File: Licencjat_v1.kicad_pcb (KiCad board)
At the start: 2 copper layers, 163 x 65 mm, 71 parts, among them J1 PV_IN_1, J10 SERIAL, J2 PV_IN_2, J3 AHT20 + BMP280, J4 VEML7700, J5 ADDITIONAL I2C, J6 RF_TRANSMITTER, J7 AVR-ISP-6, J8 GEIGER, J9 1_WIRE, Q1 AO3401A, Q10 2SC1945, Q11 AO3400A, Q2 BC846, Q3 AO3401A, Q4 AO3400A, Q5 AO3400A, Q6 AO3400A, Q7 AO3401A, Q8 AO3401A, Q9 2SC1945, U1 ATmega328P-A, U2 XC6206PxxxMR, U3 HT75xx-1-SOT89, Y1 Crystal_Small

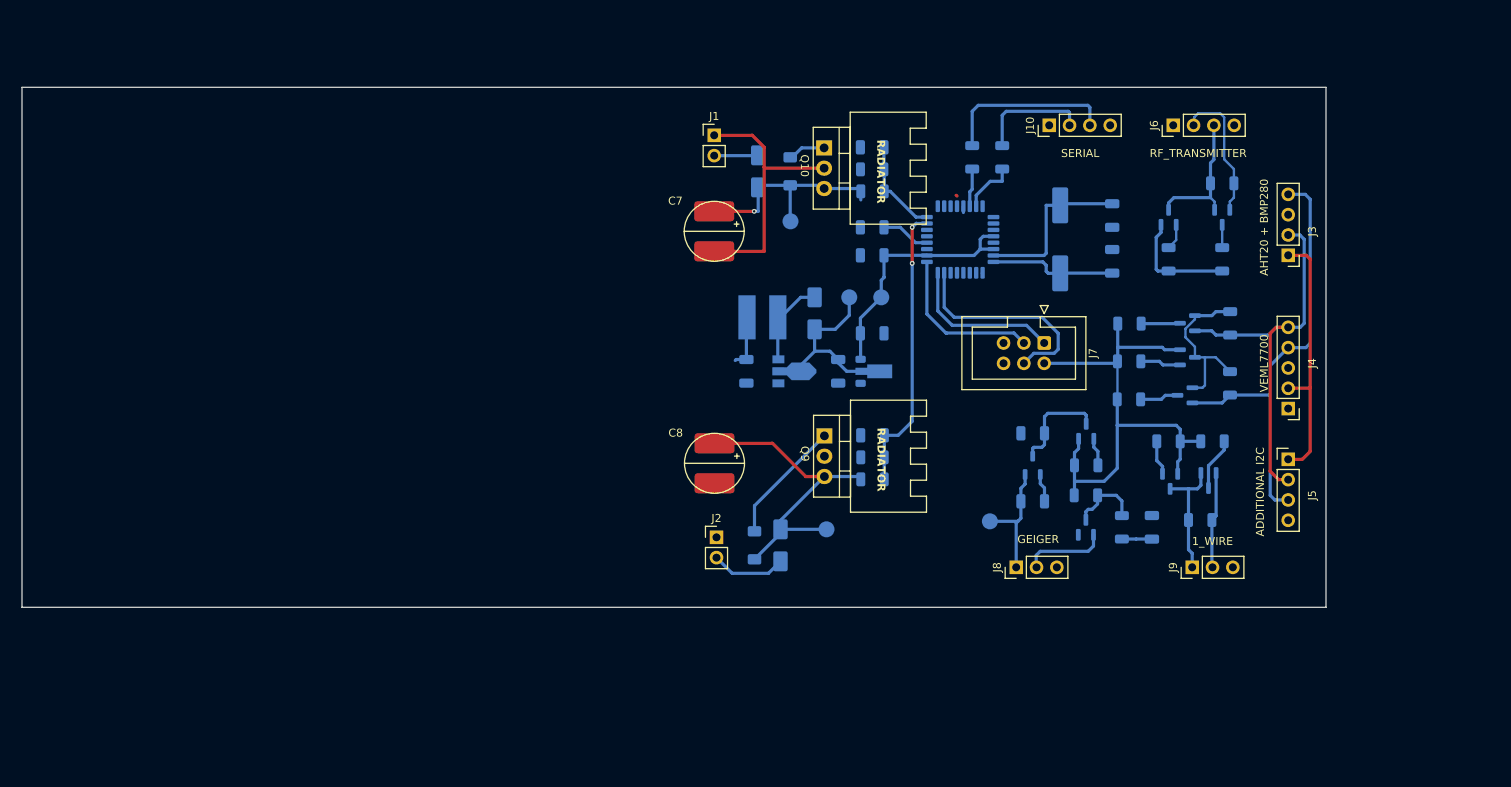
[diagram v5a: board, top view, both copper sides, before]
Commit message: Tracks placed
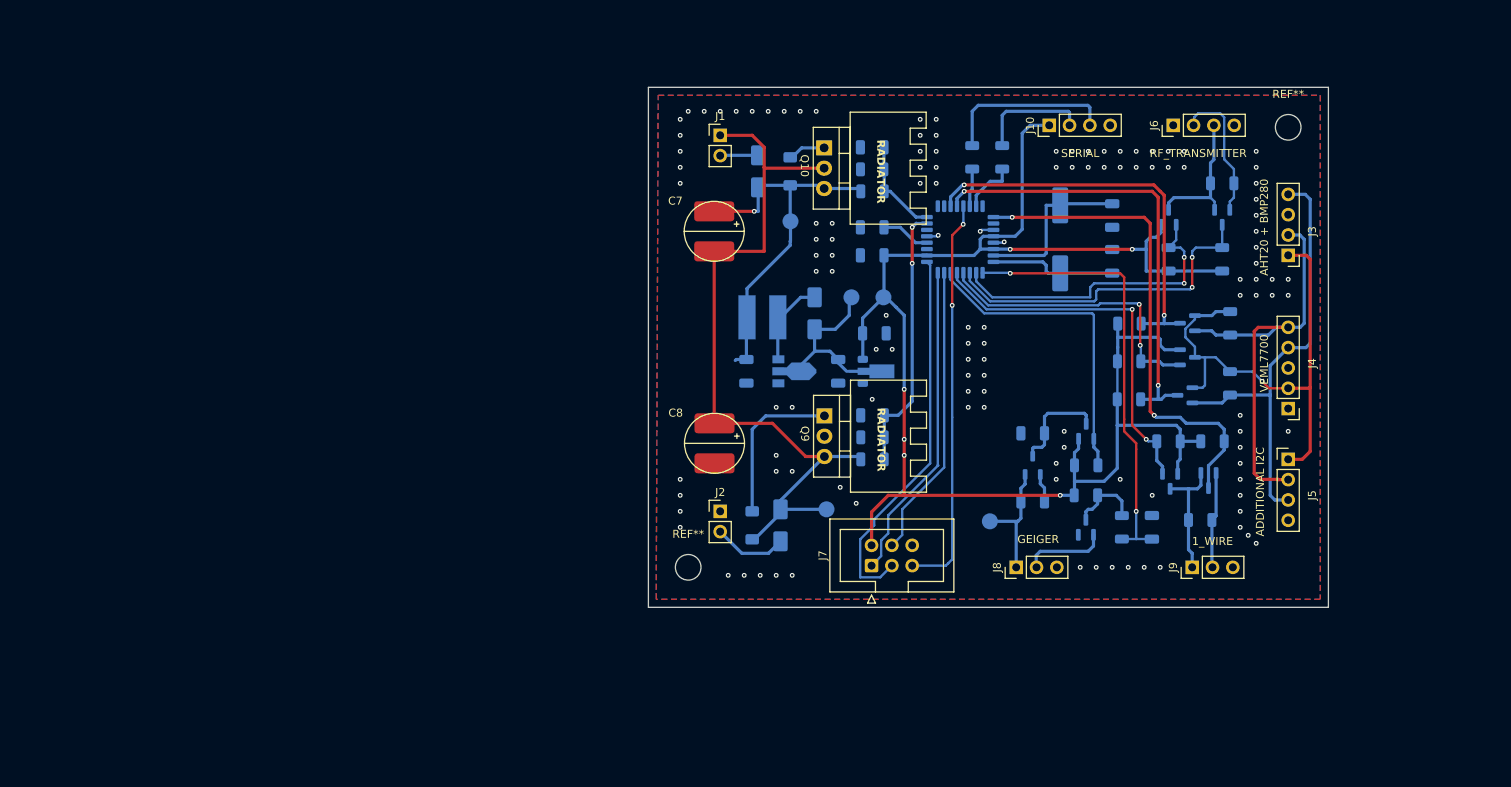
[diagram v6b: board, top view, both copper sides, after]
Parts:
- added REF**: MountingHole_3.2mm_M3, MountingHole:MountingHole_3.2mm_M3, F.Cu at (94.0, 85.0)
- added REF**: MountingHole_3.2mm_M3, MountingHole:MountingHole_3.2mm_M3, F.Cu at (169.0, 30.0)
- moved J7 35.2 mm to (116.9, 84.8), turned to 90 degrees
- moved J2 3.28 mm to (98.0, 78.0)
- moved D2 2.52 mm to (102.0, 79.8)
- moved C13 2.50 mm to (117.0, 66.0)
- moved C8 2.50 mm to (94.8, 65.7)
- moved D5 2.50 mm to (105.5, 79.8)
- moved Q9 2.50 mm to (114.3, 63.5)
- moved R10 2.50 mm to (117.0, 71.5)
- moved R11 2.50 mm to (117.0, 68.8)
- moved TP1 2.50 mm to (111.3, 77.8)
- moved J1 0.75 mm to (98.0, 31.0)
- moved C11 0.28 mm to (117.3, 55.8)
- moved TP3 0.28 mm to (114.4, 51.2)
- moved TP4 0.28 mm to (118.4, 51.2)
- moved U3 0.28 mm to (117.8, 60.5)
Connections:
- Q1 pad 1: /D4 -> /D10
- Q11 pad 3: /D10 -> /D7
- Q3 pad 1: /D7 -> /D6
- Q7 pad 1: /D8 -> /D9
- Q8 pad 1: /D6 -> /D8
- R20 pad 1: /D8 -> /D9
- R21 pad 1: /D10 -> /D7
- R3 pad 1: /D4 -> /D10
- R5 pad 1: /D7 -> /D6
- R9 pad 1: /D6 -> /D8
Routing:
- net /VCC: track 110.4 -> 199.9 mm, vias 0 -> 6
- net /1_WIRE: track 6.65 -> 61.7 mm, vias 0 -> 2
- net /SCL: track 4.95 -> 56.9 mm, vias 0 -> 2
- net /D5/T1: track 3.83 -> 55.1 mm, vias 0 -> 2
- net /~{RESET}: track 0.79 -> 50.0 mm, vias 0 -> 2
- net /D9: track 0.00 -> 47.1 mm, vias 0 -> 2
- net /SDA: track 4.87 -> 49.9 mm, vias 0 -> 2
- net /D7: track 3.24 -> 42.5 mm, vias 0 -> 2
- net /D10: track 2.90 -> 39.6 mm
- net /D6: track 5.07 -> 38.7 mm, vias 0 -> 2
- net /D8: track 4.37 -> 36.7 mm, vias 0 -> 2
- net /D13/SCK: track 20.2 -> 47.8 mm
- net /V_HALF_CAP: track 73.5 -> 94.3 mm
- net /D12/MISO: track 19.7 -> 40.1 mm
- net /V_CAP: track 34.5 -> 47.7 mm
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- added copper zone on B.Cu, net GND
- added copper zone on F.Cu, net GND
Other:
- board size 163 x 65 mm -> 85 x 65 mm
- board text added: "VCC"
- board text added: "V_BOOST"

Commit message: Labels placed
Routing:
- net /V_CAP: track 47.7 -> 46.3 mm
- net GND: vias 124 -> 127
- net /VCC: vias 6 -> 4
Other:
- board text added: "+"
- board text added: "VCC_GEIGER"
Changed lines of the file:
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@@
 		(at 94.75 39.2)
 		(property "Reference" "C7"
-			(at -2.35 0 0)
+			(at 2.5 9.3 0)
 			(unlocked yes)
 			(layer "F.SilkS")
@@
 			(layer "F.SilkS")
 		)
-		(fp_circle
-			(center 2.5 3.8)
-			(end 6.25 3.85)
+		(fp_arc
+			(start -0.357241 6.191133)
+			(mid -1.25 3.781118)
+			(end -0.381554 1.362236)
+			(stroke
+				(width 0.1)
+				(type default)
+			)
+			(layer "F.SilkS")
+		)
+		(fp_arc
+			(start 5.357526 1.371103)
+			(mid 6.250285 3.781118)
+			(end 5.381839 6.2)
 			(stroke
 				(width 0.1)
 				(type default)
 			)
-			(fill no)
 			(layer "F.SilkS")
 		)
@@
 			(polygon
 				(pts
-					(xy 101.000333 43) (xy 93.499667 43) (xy 93.6 43.85) (xy 93.75 44.4) (xy 94.2 45.2) (xy 94.9 45.95)
-					(xy 95.8 46.45) (xy 96.55 46.7) (xy 97.55 46.75) (xy 98.5 46.55) (xy 99.6 45.95) (xy 100.15 45.4)
-					(xy 100.8 44.3) (xy 101 43.45)
+					(xy 101.000332 43) (xy 101.000332 43.4) (xy 100.75 44.3) (xy 100.45 45) (xy 100.131837 45.4) (xy 99.85 45.4)
+					(xy 99.85 44.1) (xy 94.65 44.1) (xy 94.65 45.4) (xy 94.392759 45.391133) (xy 93.95 44.8) (xy 93.65 44)
+					(xy 93.55 43.3) (xy 93.500144 43) (xy 101.000426 43)
 				)
 			)
@@
 		(at 114.25 30 -90)
 		(property "Reference" "Q10"
-			(at 4.8 5.7 270)
+			(at -1 2.5 0)
 			(unlocked yes)
 			(layer "F.SilkS")
@@
 		(at 94.7875 65.7)
 		(property "Reference" "C8"
-			(at -2.35 0 0)
+			(at 2.4625 -2.2 0)
 			(unlocked yes)
 			(layer "F.SilkS")
@@
 			(layer "F.SilkS")
 		)
-		(fp_circle
-			(center 2.5 3.8)
-			(end 6.25 3.85)
+		(fp_arc
+			(start -0.357241 6.191133)
+			(mid -1.25 3.781118)
+			(end -0.381554 1.362236)
+			(stroke
+				(width 0.1)
+				(type default)
+			)
+			(layer "F.SilkS")
+		)
+		(fp_arc
+			(start 5.357526 1.371103)
+			(mid 6.250285 3.781118)
+			(end 5.381839 6.2)
 			(stroke
 				(width 0.1)
 				(type default)
 			)
-			(fill no)
 			(layer "F.SilkS")
 		)
@@
 			(polygon
 				(pts
-					(xy 101.037833 69.5) (xy 93.537167 69.5) (xy 93.6375 70.35) (xy 93.7875 70.9) (xy 94.2375 71.7)
-					(xy 94.9375 72.45) (xy 95.8375 72.95) (xy 96.5875 73.2) (xy 97.5875 73.25) (xy 98.5375 73.05) (xy 99.6375 72.45)
-					(xy 100.1875 71.9) (xy 100.8375 70.8) (xy 101.0375 69.95)
+					(xy 101.037832 69.5) (xy 101.037832 69.9) (xy 100.7875 70.8) (xy 100.4875 71.5) (xy 100.169337 71.9)
+					(xy 99.8875 71.9) (xy 99.8875 70.6) (xy 94.6875 70.6) (xy 94.6875 71.9) (xy 94.430259 71.891133)
+					(xy 93.9875 71.3) (xy 93.6875 70.5) (xy 93.5875 69.8) (xy 93.537644 69.5) (xy 101.037926 69.5)
 				)
 			)
@@
 		(tags "mountinghole M3")
 		(property "Reference" "REF**"
-			(at 0 -4.15 0)
+			(at -0.25 -5.5 0)
 			(layer "F.SilkS")
+			(hide yes)
 			(effects
 				(font
@@
 		(tags "Through hole pin header THT 1x02 2.54mm single row")
 		(property "Reference" "J2"
-			(at 0 -2.38 0)
+			(at -0.25 -2.5 0)
 			(layer "F.SilkS")
+			(hide yes)
 			(effects
 				(font
@@
 		)
 		(property "Value" "PV_IN_2"
-			(at 0 4.92 0)
-			(layer "F.Fab")
+			(at 0 -2.75 0)
+			(layer "F.SilkS")
 			(effects
 				(font
@@
 		)
 		(fp_text user "${REFERENCE}"
-			(at 0 1.27 90)
-			(layer "F.Fab")
+			(at 0 5 180)
+			(layer "F.SilkS")
 			(effects
 				(font
@@
 		(at 114.2875 63.5 -90)
 		(property "Reference" "Q9"
-			(at 4.8 5.7 270)
+			(at -1.5 2.2875 0)
 			(unlocked yes)
 			(layer "F.SilkS")
@@
 		)
 		(property "Value" "PV_IN_1"
-			(at 0 4.92 0)
-			(layer "F.Fab")
+			(at 0 5.25 0)
+			(layer "F.SilkS")
 			(effects
 				(font
@@
 		(tags "resistor")
 		(property "Reference" "R1"
-			(at 0 1.83 90)
+			(at 3.5 0 180)
 			(layer "B.SilkS")
 			(effects
@@
 		(tags "resistor")
 		(property "Reference" "R20"
-			(at 0 1.83 0)
+			(at 0.2125 -2 0)
 			(layer "B.SilkS")
 			(effects
@@
 		(tags "SOT TO_SOT_SMD")
 		(property "Reference" "U2"
-			(at 0 2.4 90)
+			(at -0.25 -3.5625 180)
 			(layer "B.SilkS")
 			(effects
@@
 		(tags "SOT TO_SOT_SMD")
 		(property "Reference" "Q2"
-			(at 0 2.4 90)
+			(at -3 0.0375 180)
 			(layer "B.SilkS")
 			(effects
@@
 		(tags "resistor")
 		(property "Reference" "R22"
-			(at 0 1.83 0)
+			(at -4 -0.25 0)
 			(layer "B.SilkS")
 			(effects
@@
 		(tags "resistor")
 		(property "Reference" "R19"
-			(at 0 1.83 0)
+			(at 0 2.0875 0)
 			(layer "B.SilkS")
 			(effects
@@
 		(tags "SOT TO_SOT_SMD")
 		(property "Reference" "Q11"
-			(at 0 2.4 90)
+			(at -0.25 -3.25 180)
 			(layer "B.SilkS")
 			(effects
@@
 		(tags "SOT TO_SOT_SMD")
 		(property "Reference" "Q5"
-			(at 0 2.4 0)
+			(at 3.09375 0 0)
 			(layer "B.SilkS")
 			(effects
@@
 		(tags "SOT TO_SOT_SMD")
 		(property "Reference" "Q7"
-			(at 0 2.4 90)
+			(at 0 2.9875 180)
 			(layer "B.SilkS")
 			(effects
@@
 		(tags "SOT TO_SOT_SMD")
 		(property "Reference" "Q6"
-			(at 0 2.4 90)
+			(at -0.15 -2.9625 180)
 			(layer "B.SilkS")
 			(effects
@@
 		(tags "resistor")
 		(property "Reference" "R2"
-			(at 0 1.83 90)
+			(at 3.5 0.25 180)
 			(layer "B.SilkS")
 			(effects
@@
 		(tags "capacitor")
 		(property "Reference" "C2"
-			(at 0 1.85 90)
+			(at -3.25 0 180)
 			(layer "B.SilkS")
 			(effects
@@
 			(at 0 1.998 0)
 			(layer "B.SilkS")
+			(hide yes)
 			(effects
 				(font
@@
 		(tags "SOT TO_SOT_SMD")
 		(property "Reference" "Q3"
-			(at 0 2.4 90)
+			(at 0 2.95 180)
 			(layer "B.SilkS")
 			(effects
@@
 		(tags "SOT TO_SOT_SMD")
 		(property "Reference" "Q8"
-			(at 0 2.4 0)
+			(at -3.15625 0.25 0)
 			(layer "B.SilkS")
 			(effects
@@
 		(tags "capacitor")
 		(property "Reference" "C14"
-			(at 0 1.85 90)
+			(at -3.25 0.0375 180)
 			(layer "B.SilkS")
 			(effects
@@
 		(tags "SOT TO_SOT_SMD")
 		(property "Reference" "Q4"
-			(at 0 2.4 0)
+			(at 3.15625 -0.0125 0)
 			(layer "B.SilkS")
 			(effects
@@
 		(tags "SOT TO_SOT_SMD")
 		(property "Reference" "Q1"
-			(at 0 2.4 90)
+			(at 0 3.25 180)
 			(layer "B.SilkS")
 			(effects
@@
 		(tags "resistor")
 		(property "Reference" "R14"
-			(at 0 1.83 90)
+			(at 0 2.75 180)
 			(layer "B.SilkS")
 			(effects
@@
 		(tags "resistor")
 		(property "Reference" "R4"
-			(at 0 1.83 0)
+			(at 3.5375 0 0)
 			(layer "B.SilkS")
 			(effects
@@
 		(tags "resistor")
 		(property "Reference" "R5"
-			(at 0 1.83 90)
+			(at 0 -2.45 180)
 			(layer "B.SilkS")
 			(effects
@@
 		(tags "resistor")
 		(property "Reference" "R21"
-			(at 0 1.83 90)
+			(at -0.25 -2.75 180)
 			(layer "B.SilkS")
 			(effects
@@
 		(tags "capacitor")
 		(property "Reference" "C9"
-			(at 0 2.125 90)
+			(at -3.25 0 180)
 			(layer "B.SilkS")
 			(effects
@@
 		(tags "resistor")
 		(property "Reference" "R16"
-			(at 0 1.83 90)
+			(at 0 2.775 180)
 			(layer "B.SilkS")
 			(effects
@@
 		(tags "capacitor")
 		(property "Reference" "C5"
-			(at 0 1.85 0)
+			(at 3.5625 0 0)
 			(layer "B.SilkS")
 			(effects
@@
 		(tags "resistor")
 		(property "Reference" "R3"
-			(at 0 1.83 0)
+			(at -3.5 0 0)
 			(layer "B.SilkS")
 			(effects
@@
 		(tags "capacitor")
 		(property "Reference" "C1"
-			(at 0 1.85 90)
+			(at -3.275 0 180)
 			(layer "B.SilkS")
 			(effects
@@
 		(tags "capacitor")
 		(property "Reference" "C6"
-			(at 0 1.85 0)
+			(at 0 2 0)
 			(layer "B.SilkS")
 			(effects
@@
 		(tags "resistor")
 		(property "Reference" "R17"
-			(at 0 1.83 90)
+			(at -3.25 0.0375 180)
 			(layer "B.SilkS")
 			(effects
@@
 		(layer "Edge.Cuts")
 	)
+	(gr_text "+"
+		(at 94.6 34.2 0)
+		(layer "F.SilkS")
+		(effects
+			(font
+				(size 1 1)
+				(thickness 0.2)
+				(bold yes)
+			)
+			(justify left bottom)
+		)
+	)
+	(gr_text "+"
+		(at 94.5 81.2 0)
+		(layer "F.SilkS")
+		(effects
+			(font
+				(size 1 1)
+				(thickness 0.2)
+				(bold yes)
+			)
+			(justify left bottom)
+		)
+	)
 	(gr_text "VCC"
 		(at 123 52 0)
@@
 		)
 	)
+	(gr_text "VCC_GEIGER"
+		(at 134.25 77.5 0)
+		(layer "B.SilkS")
+		(effects
+			(font
+				(size 1 1)
+				(thickness 0.15)
+			)
+			(justify left bottom mirror)
+		)
+	)
 	(segment
 		(start 138.477499 46.022501)
@@
 	)
 	(via
+		(at 115.5 74.5)
+		(size 0.6)
+		(drill 0.3)
+		(layers "F.Cu" "B.Cu")
+		(free yes)
+		(net 2)
+	)
+	(via
 		(at 125 33)
 		(size 0.6)
@@
 	)
 	(via
+		(at 122.75 66.75)
+		(size 0.6)
+		(drill 0.3)
+		(layers "F.Cu" "B.Cu")
+		(free yes)
+		(net 2)
+	)
+	(via
 		(at 163 74)
 		(size 0.6)
@@
 	)
 	(via
+		(at 122.75 70)
+		(size 0.6)
+		(drill 0.3)
+		(layers "F.Cu" "B.Cu")
+		(free yes)
+		(net 2)
+	)
+	(via
 		(at 143 85)
 		(size 0.6)
@@
 		(net 5)
 	)
-	(via
-		(at 121 71)
-		(size 0.6)
-		(drill 0.3)
-		(layers "F.Cu" "B.Cu")
-		(net 5)
-	)
-	(via
-		(at 121 69)
-		(size 0.6)
-		(drill 0.3)
-		(layers "F.Cu" "B.Cu")
-		(net 5)
-	)
 	(segment
 		(start 121 53.5)
@@
 	)
 	(segment
-		(start 99.88125 59.14375)
-		(end 100 59.025)
-		(width 0.4)
-		(layer "B.Cu")
-		(net 7)
-	)
-	(segment
 		(start 101.35 50.15)
 		(end 106.75 44.75)
@@
 		(width 0.4)
 		(layer "B.Cu")
-		(net 7)
-	)
-	(segment
-		(start 101.275 59.025)
-		(end 100 59.025)
-		(width 0.4)
-		(layer "B.Cu")

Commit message: More labels
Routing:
- net /D12/MISO: track 40.1 -> 42.9 mm
- net /D13/SCK: track 47.8 -> 50.1 mm
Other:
- board text added: "-"
- board text added: "CLK"
- board text added: "D"
- board text added: "RX"
- board text added: "TX"
